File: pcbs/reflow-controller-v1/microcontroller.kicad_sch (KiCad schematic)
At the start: 1 part, among them U3 STM32U575VITx

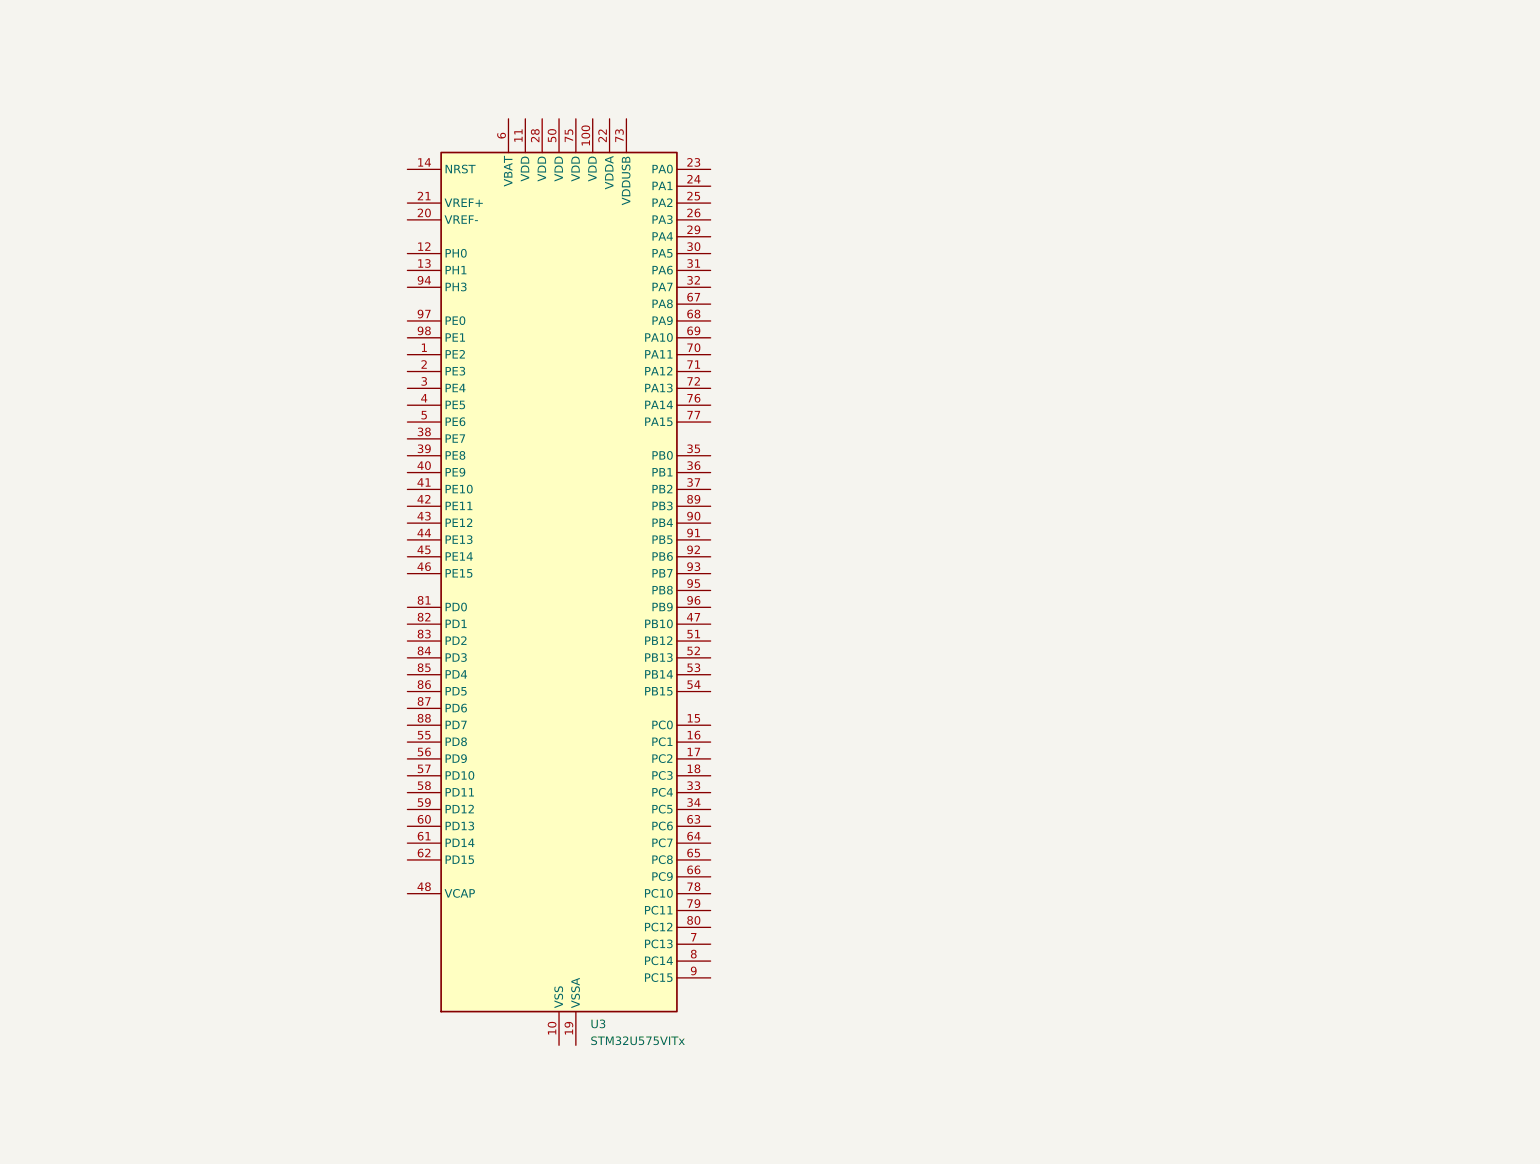
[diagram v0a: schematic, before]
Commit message: footprint assignement fixed; buzzer added
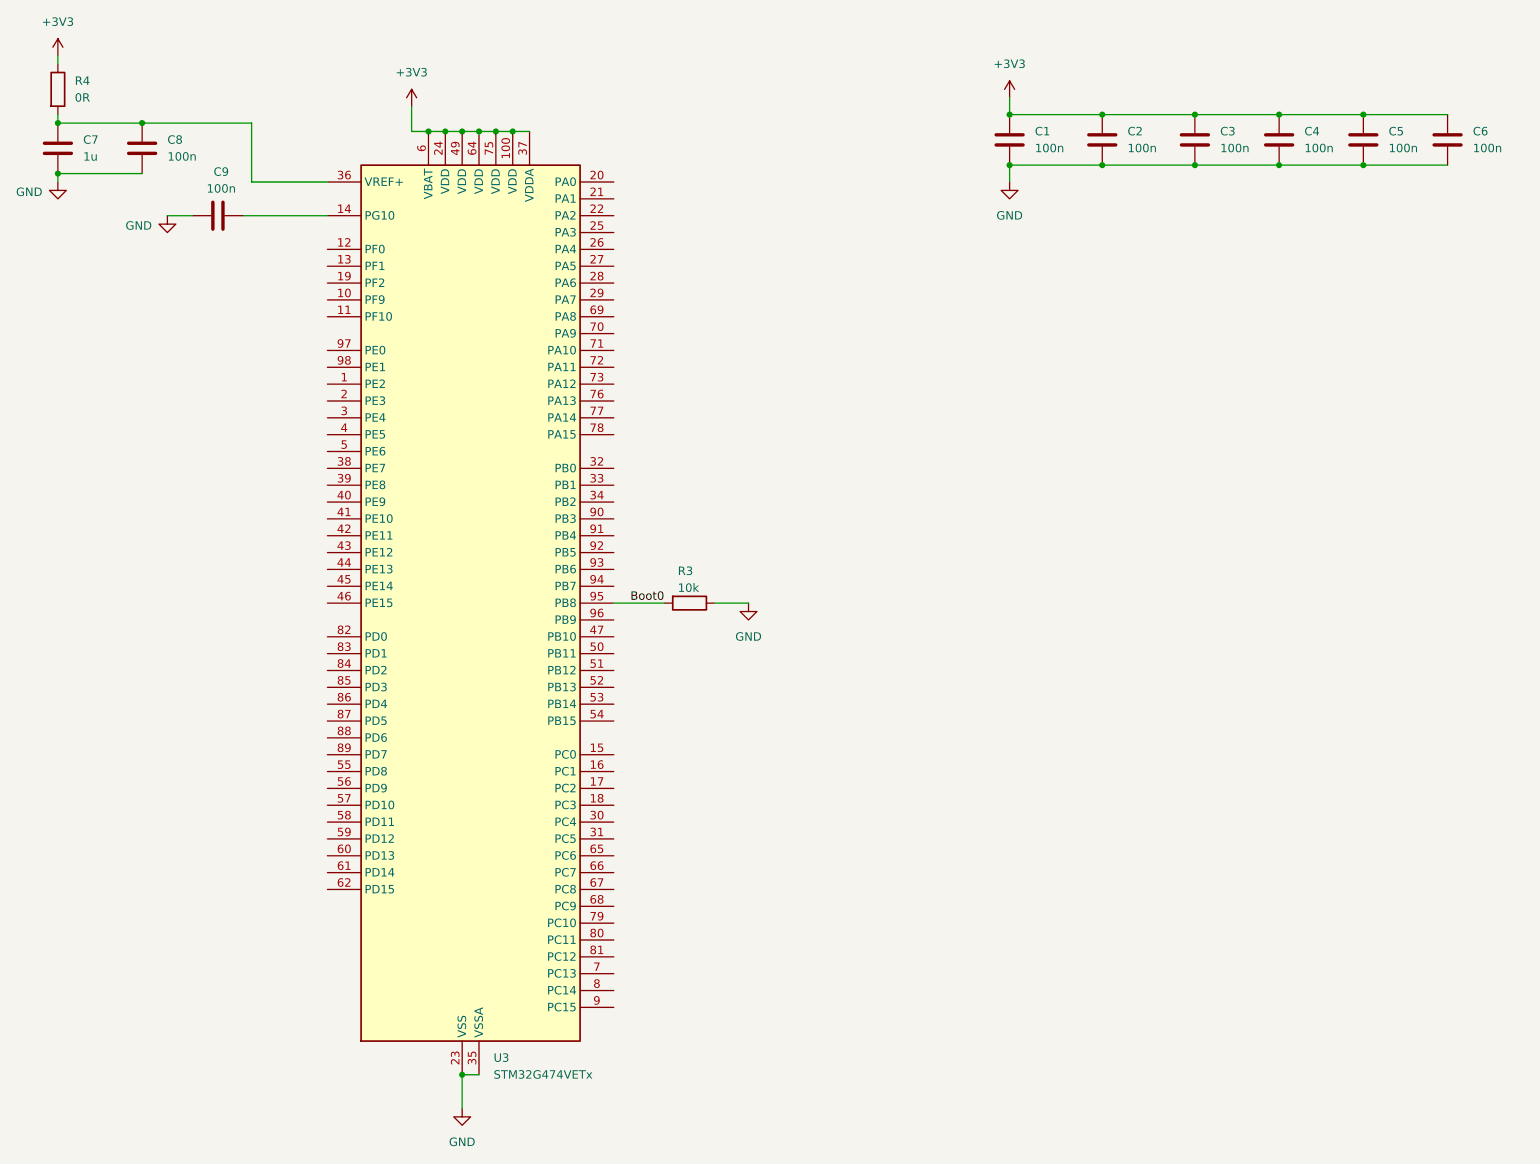
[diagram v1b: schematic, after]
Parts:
- removed U3: STM32U575VITx, Package_QFP:LQFP-100_14x14mm_P0.5mm, symbol MCU_ST_STM32U5:STM32U575VITx
- added C1, C2, C3, C4, C5, C6, C8, C9: 100n, Capacitor_SMD:C_0603_1608Metric, symbol Device:C
- added C7: 1u, Capacitor_SMD:C_0603_1608Metric, symbol Device:C
- added R3: 10k, Resistor_SMD:R_0603_1608Metric, symbol Device:R
- added R4: 0R, Resistor_SMD:R_0603_1608Metric, symbol Device:R
- added U3: STM32G474VETx, Package_QFP:LQFP-100_14x14mm_P0.5mm, symbol MCU_ST_STM32G4:STM32G474VETx
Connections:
- new net: C9.2, U3.14 (PG10)
- new net: C7.1, C8.1, R4.2, U3.36 (VREF+)
- new net +3V3: C1.1, C2.1, C3.1, C4.1, C5.1, C6.1, R4.1, U3.100 (VDD), U3.24 (VDD), U3.37 (VDDA), U3.49 (VDD), U3.6 (VBAT), U3.64 (VDD), U3.75 (VDD)
- new net Boot0: R3.2, U3.95 (PB8)
- new net GND: C1.2, C2.2, C3.2, C4.2, C5.2, C6.2, C7.2, C8.2, C9.1, R3.1, U3.23 (VSS), U3.35 (VSSA), U3.48 (VSS), U3.63 (VSS), U3.74 (VSS), U3.99 (VSS)

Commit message: WIP pcb design & routing
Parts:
- added C10: 100n, Capacitor_SMD:C_0603_1608Metric, symbol Device:C
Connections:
- net +3V3: now also C10.1
- net GND: now also C10.2
- net Temp_SPI_SCK: now reaches U3.1 (PE2)
- net ~{Temp_DRDY1}: now reaches U3.10 (PF9)
- net ~{Temp_CS1}: now reaches U3.11 (PF10)
- net ~{Temp_DRDY2}: now reaches U3.12 (PF0)
- net ~{Temp_CS2}: now reaches U3.13 (PF1)
- net PWM_1: now reaches U3.15 (PC0)
- net PWM_2: now reaches U3.16 (PC1)
- net PWM_3: now reaches U3.17 (PC2)
- net LED_green: now reaches U3.26 (PA4)
- net LED_red: now reaches U3.27 (PA5)
- net Buzzer: now reaches U3.3 (PE4)
- net Temp_SPI_MISO: now reaches U3.4 (PE5)
- net Temp_SPI_MOSI: now reaches U3.5 (PE6)
- net BTN_2: now reaches U3.50 (PB11)
- net SW_Encoder: now reaches U3.51 (PB12)
- net SD_SCK: now reaches U3.52 (PB13)
- net SD_MISO: now reaches U3.53 (PB14)
- net SD_MOSI: now reaches U3.54 (PB15)
- net Touch: now reaches U3.55 (PD8)
- net BTN_1: now reaches U3.56 (PD9)
- net SSR2: now reaches U3.57 (PD10)
- net SSR4: now reaches U3.58 (PD11)
- net Encoder_A: now reaches U3.59 (PD12)
- net Encoder_B: now reaches U3.60 (PD13)
- net SSR1: now reaches U3.61 (PD14)
- net SSR3: now reaches U3.62 (PD15)
- net OLED2_I2C_SCL: now reaches U3.65 (PC6)
- net OLED2_I2C_SDA: now reaches U3.66 (PC7)
- net OLED1_I2C_SCL: now reaches U3.67 (PC8)
- net OLED1_I2C_SDA: now reaches U3.68 (PC9)
- net Temp_I2C_SDA: now reaches U3.69 (PA8)
- net Temp_I2C_SCL: now reaches U3.70 (PA9)
- net Touch_SPI_IRQ: now reaches U3.78 (PA15)
- net Touch_SPI_SCK: now reaches U3.79 (PC10)
- net ~{Temp_DRDY3}: now reaches U3.8 (PC14)
- net Touch_SPI_MISO: now reaches U3.80 (PC11)
- net Touch_SPI_MOSI: now reaches U3.81 (PC12)
- net Touch_SPI_CS: now reaches U3.82 (PD0)
- net DISP_LED: now reaches U3.89 (PD7)
- net ~{Temp_CS3}: now reaches U3.9 (PC15)
- net Display_SPI_SCK: now reaches U3.90 (PB3)
- net Display_SPI_MISO: now reaches U3.91 (PB4)
- net Display_SPI_MOSI: now reaches U3.92 (PB5)
- net Display_SPI_DC/RS: now reaches U3.93 (PB6)
- net ~{Display_RESET}: now reaches U3.94 (PB7)
- net ~{Display_CS}: now reaches U3.97 (PE0)
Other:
- note added: "SPI1"
- note added: "SPI2"
- note added: "SPI3"
- note added: "SPI4"
- moved on the sheet: C1, C2, C3, C4, C5, C6

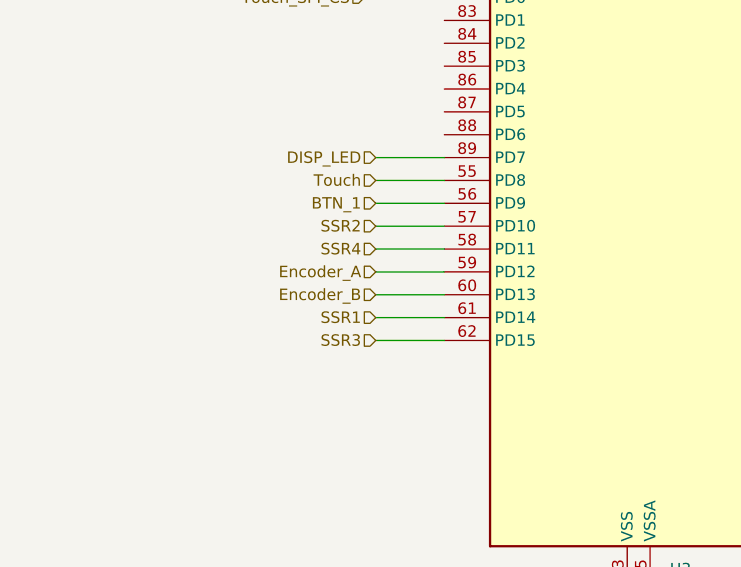
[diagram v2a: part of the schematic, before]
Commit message: update routing with new mechanical positioning
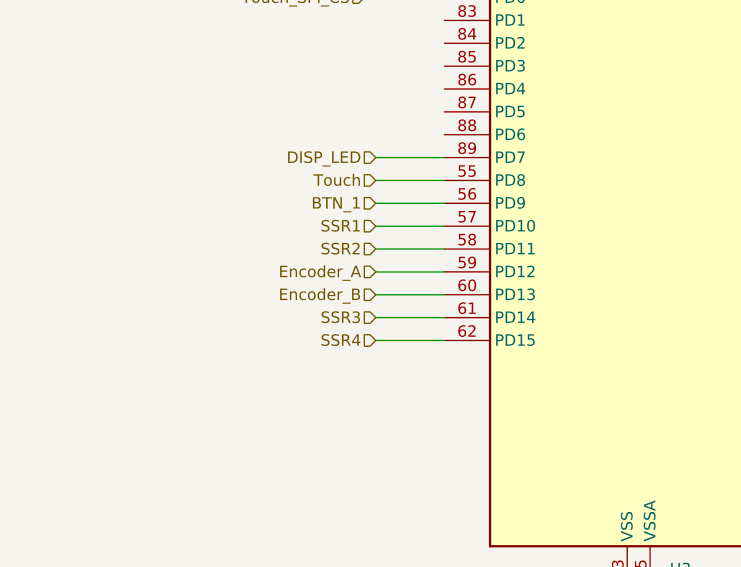
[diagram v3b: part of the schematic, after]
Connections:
- net SSR1: now also U3.57 (PD10); no longer U3.61 (PD14)
- net SSR2: now also U3.58 (PD11); no longer U3.57 (PD10)
- net SSR3: now also U3.61 (PD14); no longer U3.62 (PD15)
- net SSR4: now also U3.62 (PD15); no longer U3.58 (PD11)
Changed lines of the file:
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@@
 	(hierarchical_label "SSR4"
 		(shape input)
+		(at 93.98 146.05 180)
+		(fields_autoplaced yes)
+		(effects
+			(font
+				(size 1.27 1.27)
+			)
+			(justify right)
+		)
+	)
+	(hierarchical_label "SSR2"
+		(shape input)
 		(at 93.98 135.89 180)
-		(fields_autoplaced yes)
-		(effects
-			(font
-				(size 1.27 1.27)
-			)
-			(justify right)
-		)
-	)
-	(hierarchical_label "SSR2"
-		(shape input)
-		(at 93.98 133.35 180)
 		(fields_autoplaced yes)
 		(effects
@@
 	(hierarchical_label "SSR3"
 		(shape input)
-		(at 93.98 146.05 180)
+		(at 93.98 143.51 180)
 		(fields_autoplaced yes)
 		(effects
@@
 	(hierarchical_label "SSR1"
 		(shape input)
-		(at 93.98 143.51 180)
-		(fields_autoplaced yes)
-		(effects
+		(at 93.98 133.35 180)
+		(fields_autoplaced yes)
+		(effects

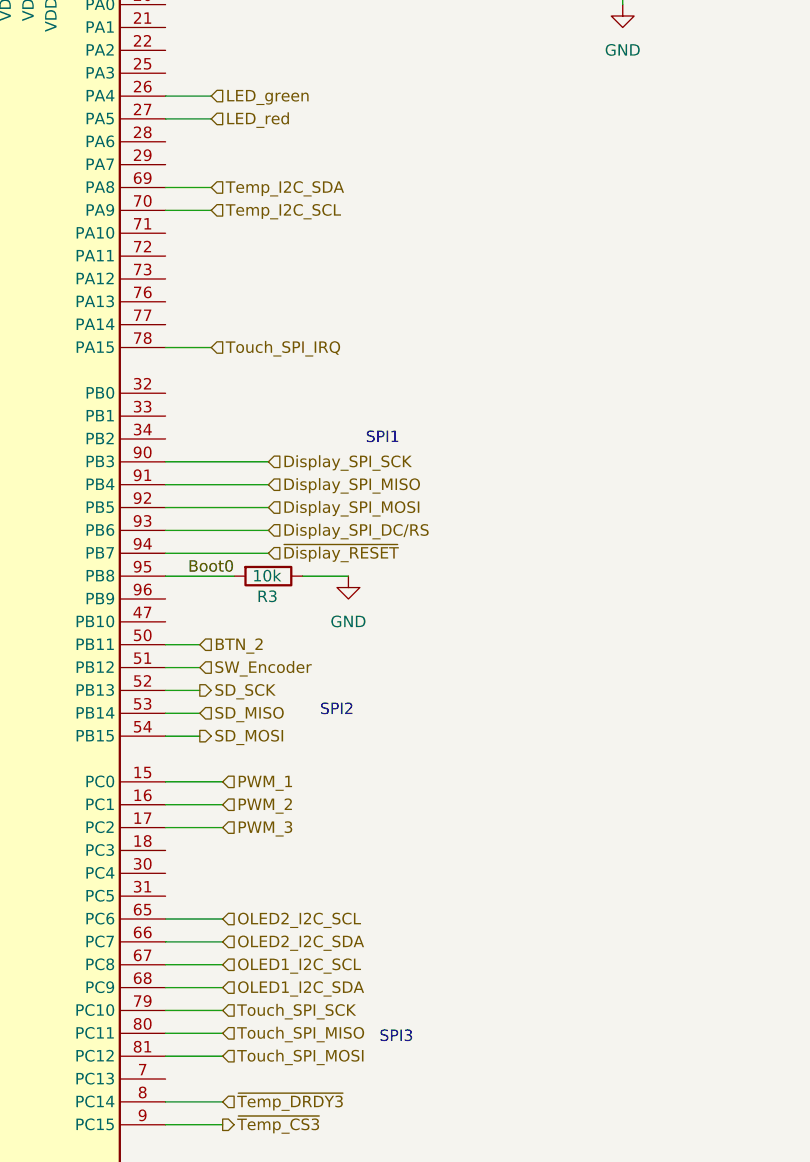
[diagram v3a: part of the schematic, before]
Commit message: add debug uart & swd
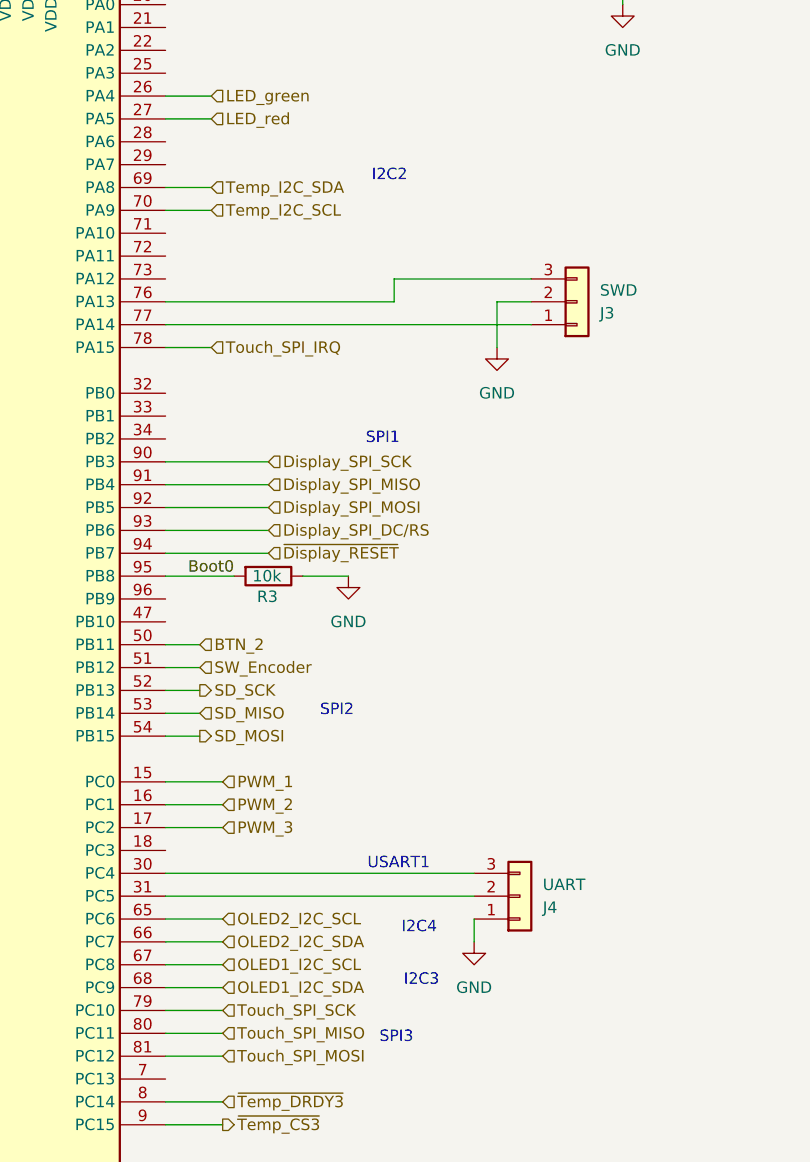
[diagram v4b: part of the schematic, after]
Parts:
- added J3: SWD, Connector_Molex:Molex_KK-254_AE-6410-03A_1x03_P2.54mm_Vertical, symbol Connector_Generic:Conn_01x03
- added J4: UART, Connector_Molex:Molex_KK-254_AE-6410-03A_1x03_P2.54mm_Vertical, symbol Connector_Generic:Conn_01x03
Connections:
- net GND: now also J3.2 (Pin_2), J4.1 (Pin_1)
- net at U3.30 (PC4): now also J4.3 (Pin_3)
- net at U3.31 (PC5): now also J4.2 (Pin_2)
- net at U3.76 (PA13): now also J3.3 (Pin_3)
- net at U3.77 (PA14): now also J3.1 (Pin_1)
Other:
- note added: "I2C2"
- note added: "I2C3"
- note added: "I2C4"
- note added: "USART1"

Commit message: label uart & swd
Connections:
- net USART1_TX: now reaches J4.3 (Pin_3), U3.30 (PC4)
- net USART1_RX: now reaches J4.2 (Pin_2), U3.31 (PC5)
- net SWDIO: now reaches J3.3 (Pin_3), U3.76 (PA13)
- net SWCLK: now reaches J3.1 (Pin_1), U3.77 (PA14)
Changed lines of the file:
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@@
 	(text "USART1"
 		(exclude_from_sim no)
-		(at 170.688 134.874 0)
+		(at 190.246 134.62 0)
 		(effects
 			(font
@@
 		)
 	)
+	(label "USART1_RX"
+		(at 163.83 138.43 0)
+		(fields_autoplaced yes)
+		(effects
+			(font
+				(size 1.27 1.27)
+			)
+			(justify left bottom)
+		)
+	)
+	(label "USART1_TX"
+		(at 163.83 135.89 0)
+		(fields_autoplaced yes)
+		(effects
+			(font
+				(size 1.27 1.27)
+			)
+			(justify left bottom)
+		)
+	)
+	(label "SWDIO"
+		(at 156.21 72.39 0)
+		(fields_autoplaced yes)
+		(effects
+			(font
+				(size 1.27 1.27)
+			)
+			(justify left bottom)
+		)
+	)
+	(label "SWCLK"
+		(at 156.21 74.93 0)
+		(fields_autoplaced yes)
+		(effects
+			(font
+				(size 1.27 1.27)
+			)
+			(justify left bottom)
+		)
+	)

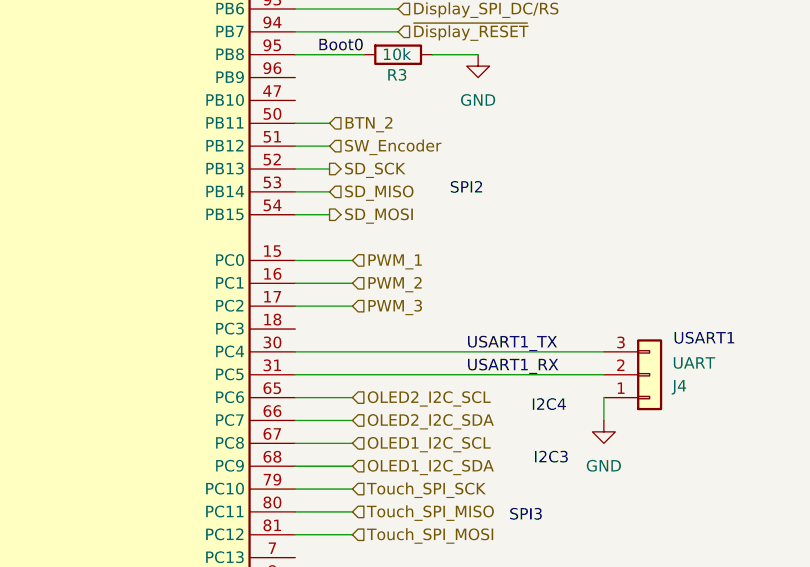
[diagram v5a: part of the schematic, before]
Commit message: move Fan PWM to different timer
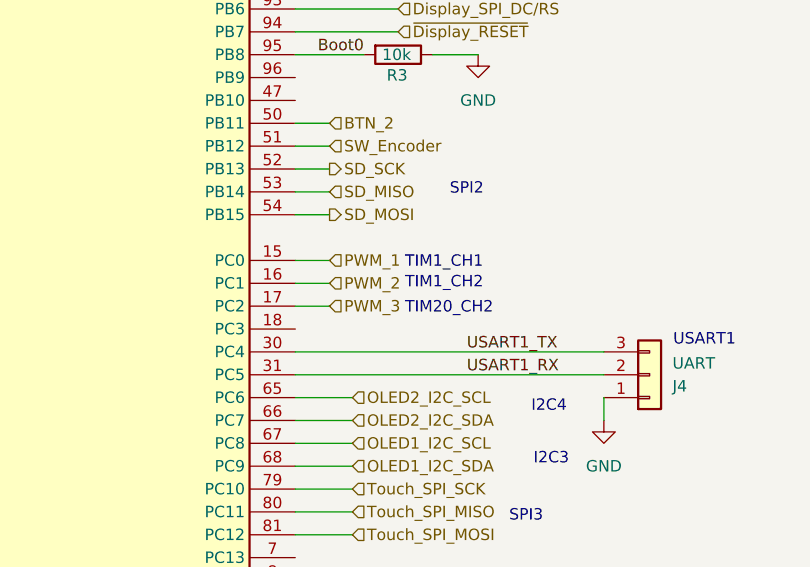
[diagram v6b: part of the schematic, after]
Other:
- note added: "TIM1_CH1"
- note added: "TIM1_CH2"
- note added: "TIM20_CH2"
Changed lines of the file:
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@@
 	(wire
 		(pts
-			(xy 144.78 128.27) (xy 151.13 128.27)
+			(xy 144.78 128.27) (xy 148.59 128.27)
 		)
 		(stroke
@@
 	(wire
 		(pts
-			(xy 144.78 125.73) (xy 151.13 125.73)
+			(xy 144.78 125.73) (xy 148.59 125.73)
 		)
 		(stroke
@@
 	(wire
 		(pts
-			(xy 144.78 130.81) (xy 151.13 130.81)
+			(xy 144.78 130.81) (xy 148.59 130.81)
 		)
 		(stroke
@@
 		)
 	)
+	(text "TIM1_CH1"
+		(exclude_from_sim no)
+		(at 156.972 125.984 0)
+		(effects
+			(font
+				(size 1.27 1.27)
+			)
+			(justify left)
+		)
+	)
 	(text "SPI3"
 		(exclude_from_sim no)
@@
 		)
 	)
+	(text "TIM1_CH2"
+		(exclude_from_sim no)
+		(at 156.972 128.27 0)
+		(effects
+			(font
+				(size 1.27 1.27)
+			)
+			(justify left)
+		)
+	)
+	(text "TIM20_CH2"
+		(exclude_from_sim no)
+		(at 156.972 131.064 0)
+		(effects
+			(font
+				(size 1.27 1.27)
+			)
+			(justify left)
+		)
+	)
 	(label "USART1_RX"
 		(at 163.83 138.43 0)
@@
 	(hierarchical_label "PWM_3"
 		(shape input)
-		(at 151.13 130.81 0)
+		(at 148.59 130.81 0)
 		(fields_autoplaced yes)
 		(effects
@@
 	(hierarchical_label "PWM_2"
 		(shape input)
-		(at 151.13 128.27 0)
+		(at 148.59 128.27 0)
 		(fields_autoplaced yes)
 		(effects
@@
 	(hierarchical_label "PWM_1"
 		(shape input)
-		(at 151.13 125.73 0)
-		(fields_autoplaced yes)
-		(effects
+		(at 148.59 125.73 0)
+		(fields_autoplaced yes)
+		(effects
